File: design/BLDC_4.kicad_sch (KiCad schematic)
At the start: 26 parts, among them K1 SERVO, P1 HALL/Encoder, P101 CANBUS, P3 PWR_COMM, P4 IN+, P5 IN-, P6 MOTOR1, P7 MOTOR2, P9 MOTOR3, X1 MINI-USB-SHIELD-32005-201

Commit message: extended board include input power caps and holes for wires
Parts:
- P4, P5: footprint CRF1:1PAD_4x5mm -> MountingHole:MountingHole_3.7mm_Pad
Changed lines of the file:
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@@
 			)
 		)
-		(property "Footprint" "CRF1:1PAD_4x5mm"
+		(property "Footprint" "MountingHole:MountingHole_3.7mm_Pad"
 			(at 227.33 35.56 0)
 			(effects
@@
 			)
 		)
-		(property "Footprint" "CRF1:1PAD_4x5mm"
+		(property "Footprint" "MountingHole:MountingHole_3.7mm_Pad"
 			(at 227.33 30.48 0)
 			(effects

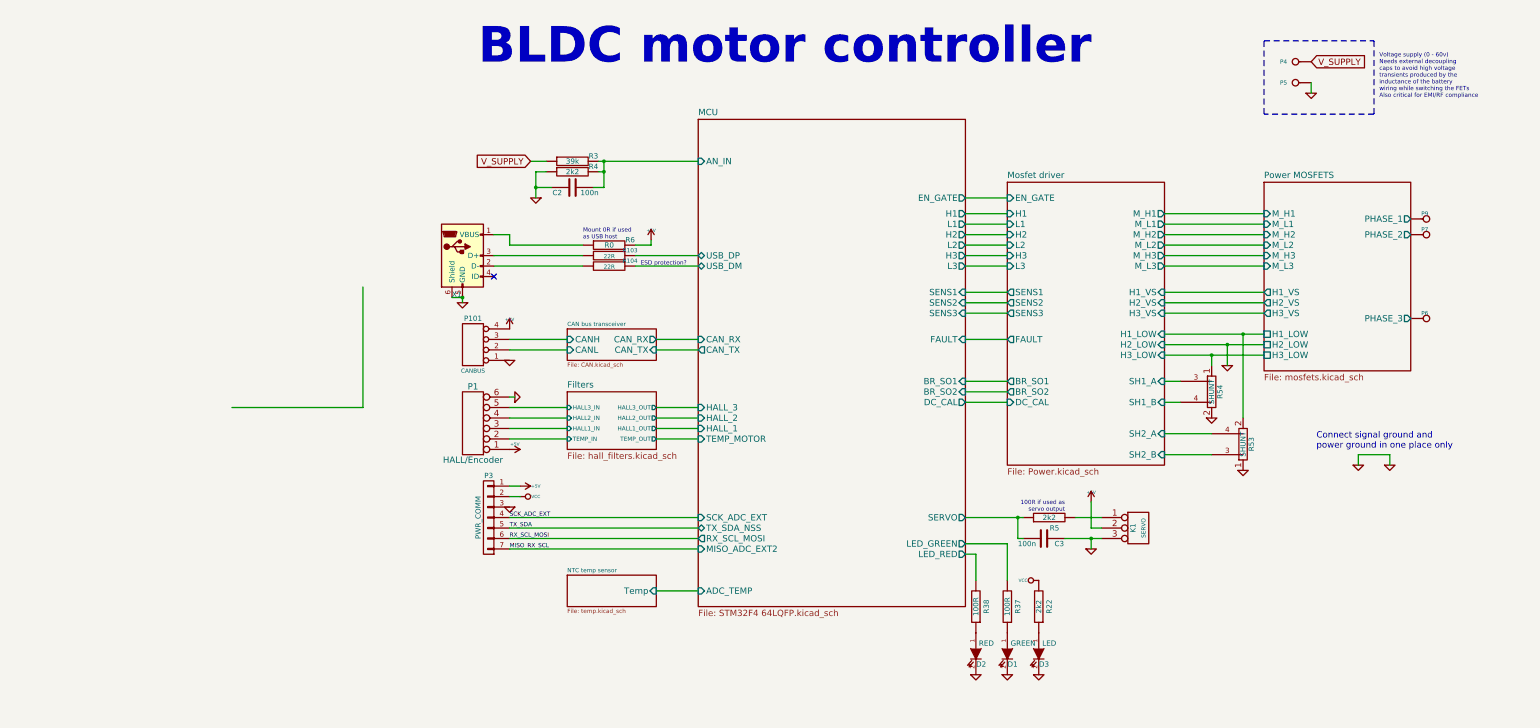
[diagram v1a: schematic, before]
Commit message: v 4.13 produced by jlcpcb
Some serious issues with usb connectors facing the caps. Working fine
otherwise
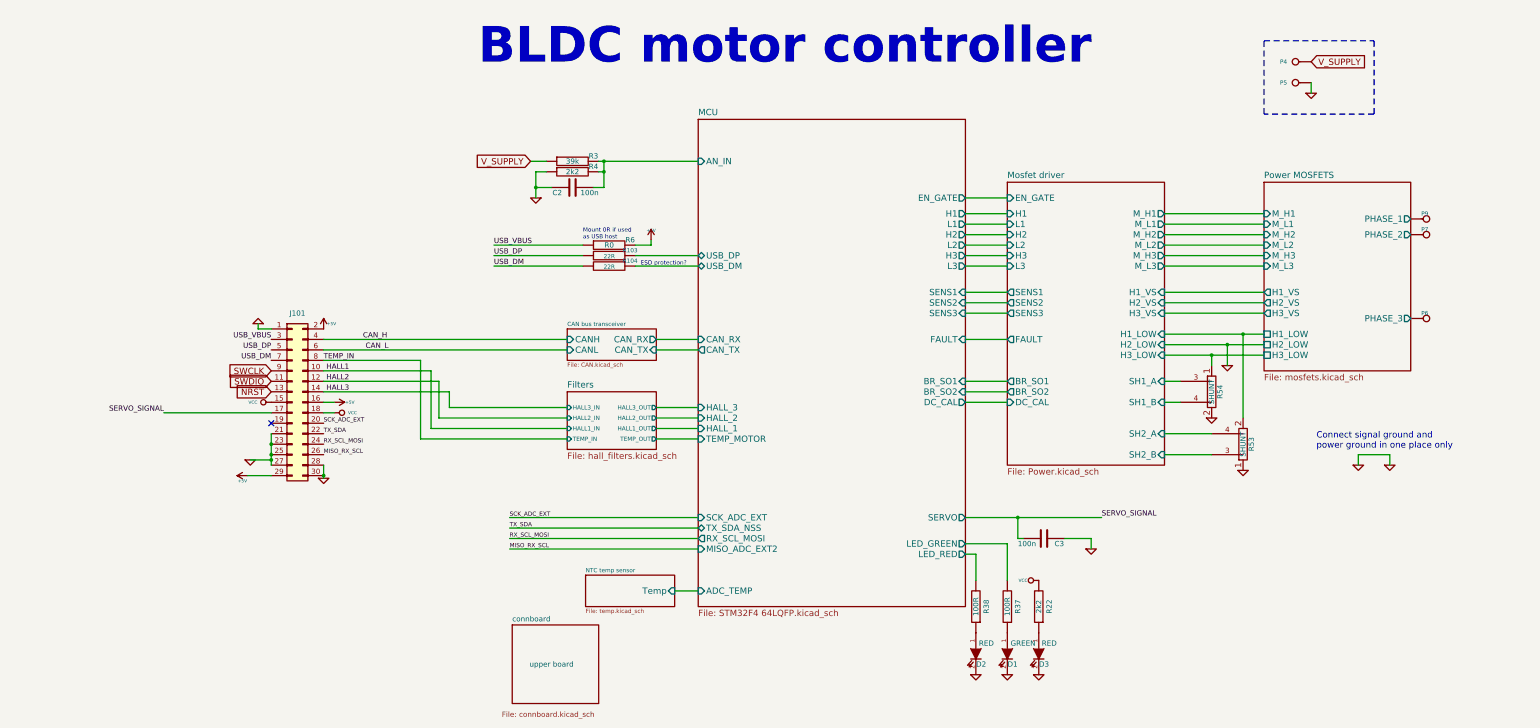
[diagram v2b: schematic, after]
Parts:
- removed K1: SERVO, CRF1:pinhead-1X03, symbol BLDC_4-rescue:CONN_3
- removed P1: HALL/Encoder, CRF1:MICRO_JST_6, symbol BLDC_4-rescue:CONN_6
- removed P101: CANBUS, JST conn:b4b-ph-kl, symbol BLDC_4-rescue:CONN_4
- removed P3: PWR_COMM, CRF1:b7b-ph-kl, symbol BLDC_4-rescue:CONN_01X07
- removed R5: 2k2, CRF1:SMD-0603_r, symbol BLDC_4-rescue:R-RESCUE-BLDC_4
- removed X1: MINI-USB-SHIELD-32005-201, Connector_USB:USB_Micro-B_Amphenol_10103594-0001LF_Horizontal, symbol Connector:USB_OTG
- added J101: Conn_02x16_Odd_Even, Connector_PinHeader_2.54mm:PinHeader_2x15_P2.54mm_Vertical, symbol Connector_Generic:Conn_02x15_Odd_Even
- D1: JLCPCB (none) -> C264448, C19273151
- D3: value LED -> RED
- R53, R54: JLCPCB (none) -> C500635
- R6: JLCPCB (none) -> C21189
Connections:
- net +5V: now also J101.16 (Pin_16), J101.2 (Pin_2), J101.29 (Pin_29)
- net GND: now also J101.1 (Pin_1), J101.21 (Pin_21), J101.23 (Pin_23), J101.25 (Pin_25), J101.27 (Pin_27), J101.28 (Pin_28), J101.30 (Pin_30)
- net MISO_RX_SCL: now also J101.26 (Pin_26)
- net RX_SCL_MOSI: now also J101.24 (Pin_24)
- net SCK_ADC_EXT: now also J101.20 (Pin_20)
- net TX_SDA: now also J101.22 (Pin_22)
- net VCC: now also J101.15 (Pin_15), J101.18 (Pin_18)
- net USB_VBUS: now reaches R6.1
- net USB_VBUS: now also J101.3 (Pin_3)
- net USB_DM: now reaches R104.2
- net USB_DM: now also J101.7 (Pin_7)
- net USB_DP: now reaches R103.2
- net USB_DP: now also J101.5 (Pin_5)
- net MCU/SERVO renamed SERVO_SIGNAL
- net SERVO_SIGNAL: now also J101.17 (Pin_17)
- new net CAN_H: J101.4 (Pin_4)
- new net CAN_L: J101.6 (Pin_6)
- new net HALL1: J101.10 (Pin_10)
- new net HALL2: J101.12 (Pin_12)
- new net HALL3: J101.14 (Pin_14)
- new net NRST: J101.13 (Pin_13)
- new net SWCLK: J101.9 (Pin_9)
- new net SWDIO: J101.11 (Pin_11)
- new net TEMP_IN: J101.8 (Pin_8)
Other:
- added sheet connboard (connboard.kicad_sch)
- note removed: "100R if used as servo output"
- note removed: "Voltage supply (0 - 60v) Needs external decoupling caps to avoid high voltage transients produced by the inductance of the battery wiring while switching the FETs Also critical for EMI/RF compliance"
- title: BLDC Driver 4.11 -> BLDC Driver 

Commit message: v4.14 Changed power connectors to XT90 and XT60
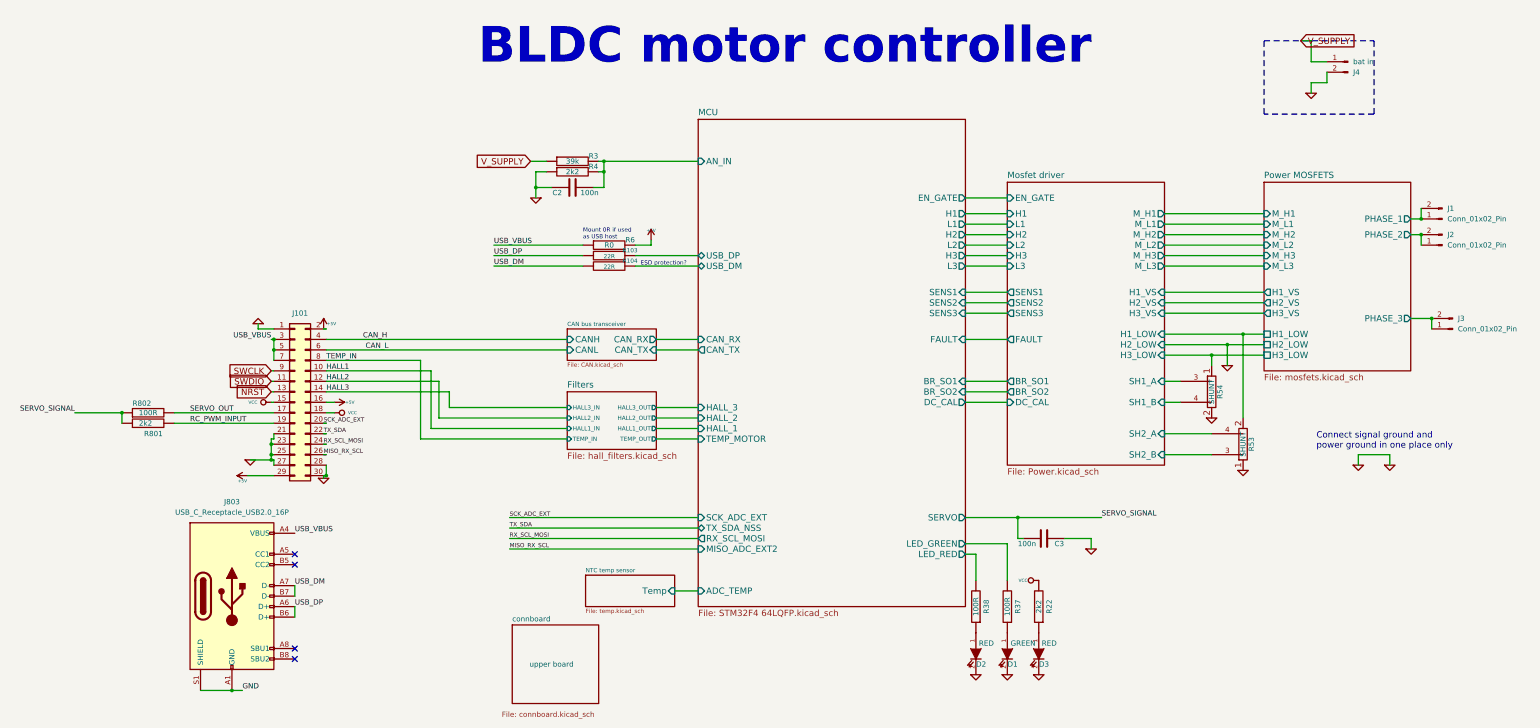
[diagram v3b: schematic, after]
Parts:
- removed P4: IN+, MountingHole:MountingHole_3.7mm_Pad, symbol BLDC_4-rescue:CONN_1
- removed P5: IN-, MountingHole:MountingHole_3.7mm_Pad, symbol BLDC_4-rescue:CONN_1
- removed P6: MOTOR1, CRF1:1PAD_4x5mm, symbol BLDC_4-rescue:CONN_1
- removed P7: MOTOR2, CRF1:1PAD_4x5mm, symbol BLDC_4-rescue:CONN_1
- removed P9: MOTOR3, CRF1:1PAD_4x5mm, symbol BLDC_4-rescue:CONN_1
- added J1, J2, J3: Conn_01x02_Pin, Connector_AMASS:AMASS_XT60-F_1x02_P7.20mm_Vertical, symbol Connector:Conn_01x02_Pin
- added J4: bat in, august:xt-90 vertical, symbol Connector:Conn_01x02_Pin
- added J803: USB_C_Receptacle_USB2.0_16P, Connector_USB:USB_C_Receptacle_GCT_USB4115-03-C, symbol Connector:USB_C_Receptacle_USB2.0_16P
- added R801: 2k2, CRF1:SMD-0603_r, symbol BLDC_4-rescue:R-RESCUE-BLDC_4
- added R802: 100R, CRF1:SMD-0603_r, symbol BLDC_4-rescue:R-RESCUE-BLDC_4
- D1: JLCPCB C264448, C19273151 -> C19273151
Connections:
- net GND: now also J4.2 (Pin_2), J803.A1 (GND), J803.A12 (GND), J803.B1 (GND), J803.B12 (GND), J803.S1 (SHIELD)
- net Power MOSFETS/PHASE_1: now also J1.1 (Pin_1), J1.2 (Pin_2)
- net Power MOSFETS/PHASE_2: now also J2.1 (Pin_1), J2.2 (Pin_2)
- net Power MOSFETS/PHASE_3: now also J3.1 (Pin_1), J3.2 (Pin_2)
- net SERVO_SIGNAL: now also R801.1, R802.1; no longer J101.17 (Pin_17)
- net USB_DM: now also J803.A7 (D-), J803.B7 (D-); no longer J101.7 (Pin_7)
- net USB_DP: now also J803.A6 (D+), J803.B6 (D+); no longer J101.5 (Pin_5)
- net USB_VBUS: now also J101.5 (Pin_5), J101.7 (Pin_7), J803.A4 (VBUS), J803.A9 (VBUS), J803.B4 (VBUS), J803.B9 (VBUS)
- net V_SUPPLY: now also J4.1 (Pin_1)
- net RC_PWM_INPUT: now reaches J101.19 (Pin_19)
- net RC_PWM_INPUT: now also R801.2
- new net SERVO_OUT: J101.17 (Pin_17), R802.2
- no-connect marks 1 -> 4
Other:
- moved on the sheet: J101
